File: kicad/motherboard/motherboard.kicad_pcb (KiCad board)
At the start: 2 copper layers, 88.9 x 80 mm, 33 parts, among them P1 CONN06, P10 CONN06, P11 CONN06, P12 CONN06, P13 CONN06, P14 CONN06, P15 CONN06, P16 CONN06, P17 CONN06, P18 CONN06, P19 CONN06, P2 CONN06, P20 CONN06, P21 CONN06, P22 CONN06, P23 CONN06, P24 CONN06, P25 CONN06, P26 CONN06, P27 CONN06, P28 CONN06, P29 CONN06, P3 CONN06, P30 CONN06, P31 CONN06, P32 CONN06, P4 CONN06, P5 CONN06, P6 CONN06, P7 CONN06, P8 CONN06, P9 CONN06

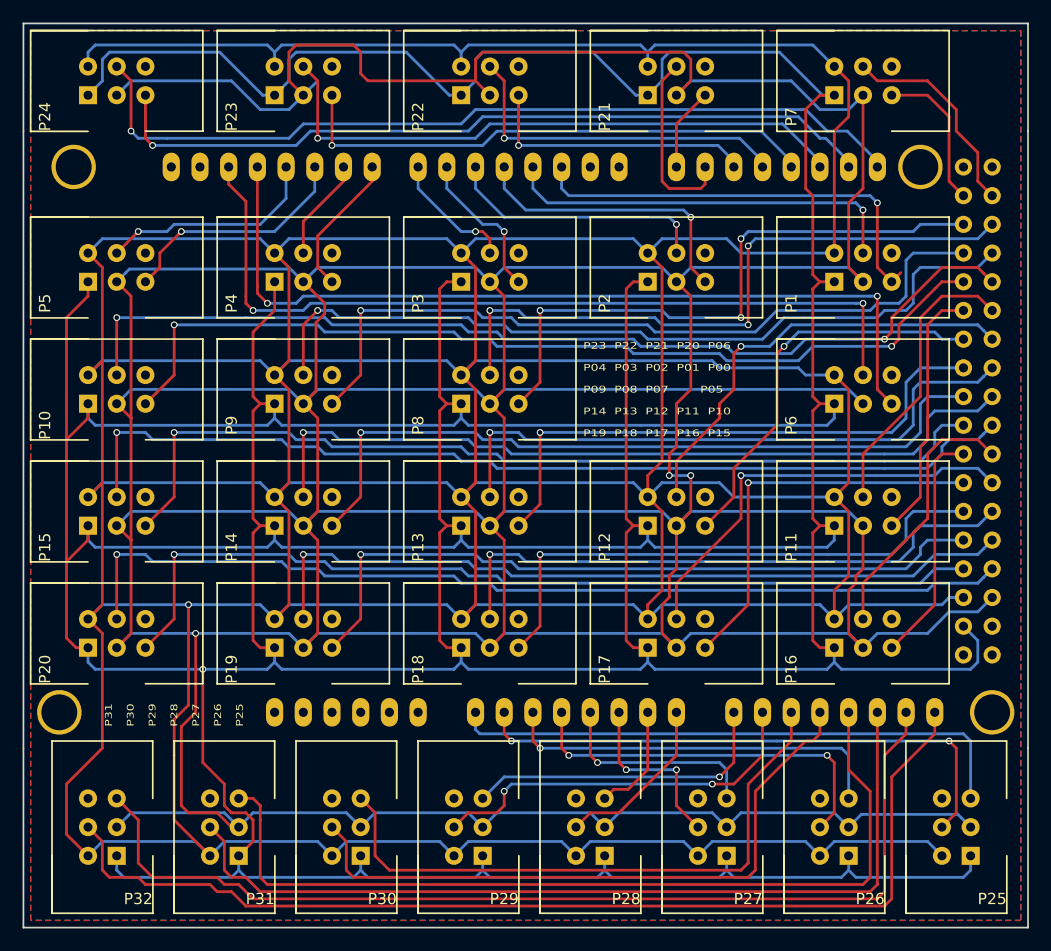
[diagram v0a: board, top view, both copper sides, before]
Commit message: Fix port references in Motherboard
So they match the port names
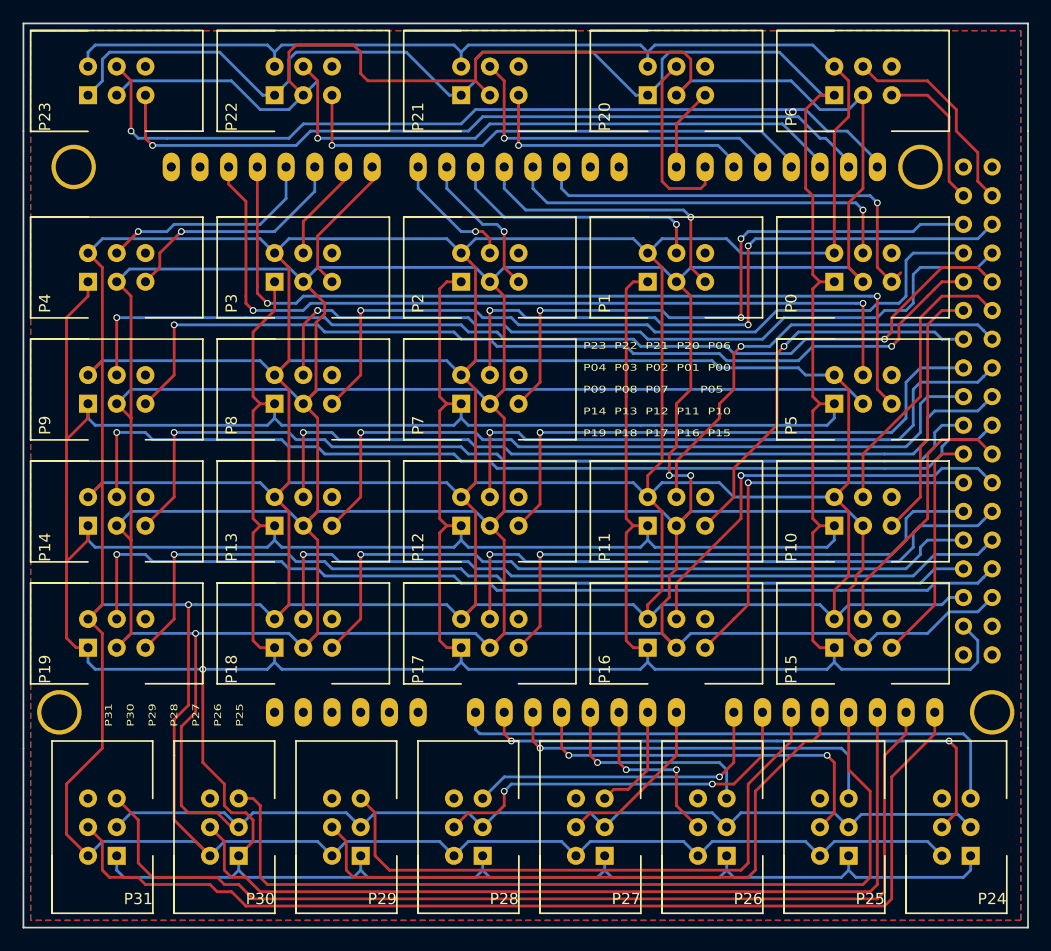
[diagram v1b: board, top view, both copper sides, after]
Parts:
- renumbered P1 to P0, P2 to P1, P11 to P10, P12 to P11, P13 to P12, P14 to P13, P15 to P14, P16 to P15, P17 to P16, P18 to P17, P19 to P18, P20 to P19, P3 to P2, P21 to P20, P22 to P21, P23 to P22, P24 to P23, P25 to P24, P26 to P25, P27 to P26, P28 to P27, P29 to P28, P30 to P29, P4 to P3, P31 to P30, P32 to P31, P5 to P4, P6 to P5, P7 to P6, P8 to P7, P9 to P8, P10 to P9

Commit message: Fix some aesthetical  paths in Motherboard
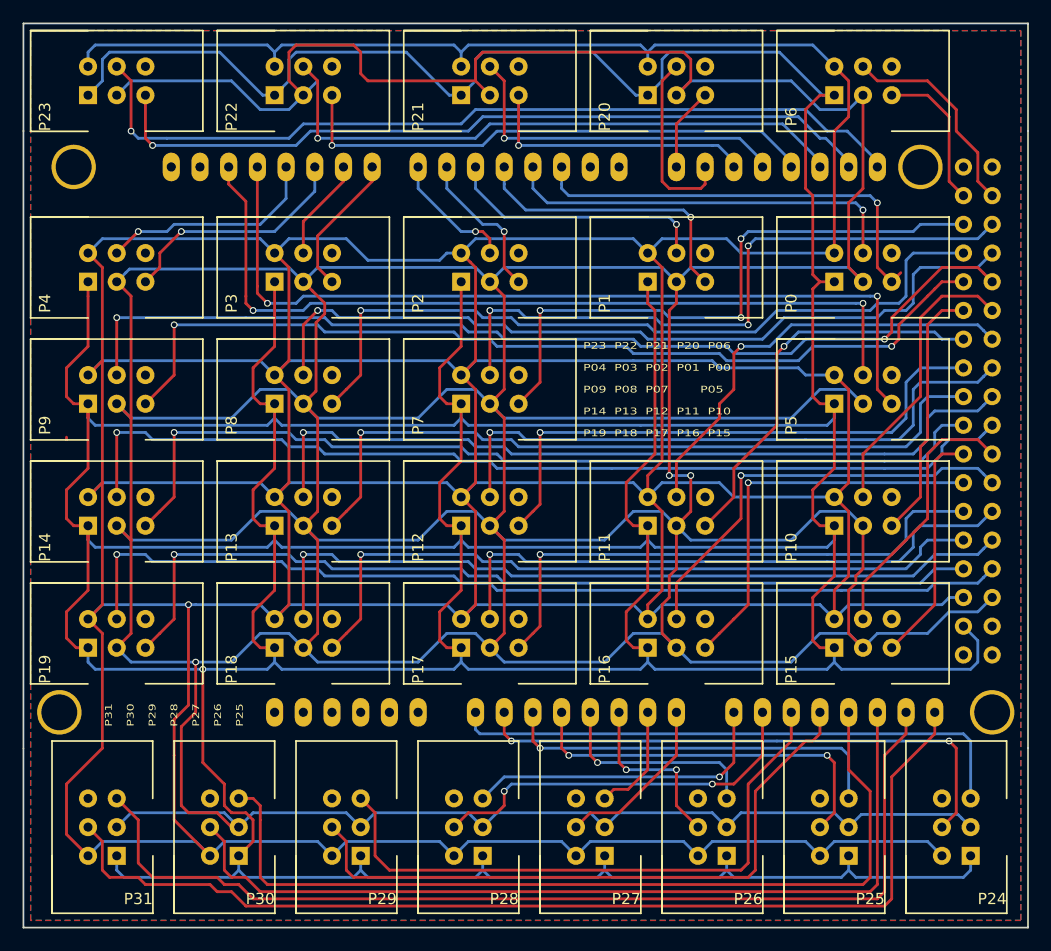
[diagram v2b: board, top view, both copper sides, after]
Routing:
- net MOSI: track 662.4 -> 670.4 mm
- net SCK: track 645.7 -> 647.7 mm
- net MISO: track 680.4 -> 680.9 mm

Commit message: Update plot settings for Motherboard
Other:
- board text added: "Avionica Motherboard for Arduino Mega - Rev.01"
- board text removed: "Avionica Motherboard Rev.01"
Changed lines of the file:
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@@
     (links 200)
     (no_connects 0)
-    (area 100.889999 74.854999 189.940001 155.015001)
+    (area 99.88 74.854999 189.940001 155.015001)
     (thickness 1.6)
     (drawings 12)
@@
     (visible_elements 7FFFF7FF)
     (pcbplotparams
-      (layerselection 0x010f0_80000001)
+      (layerselection 0x020f0_80000001)
       (usegerberextensions false)
       (excludeedgelayer true)
@@
   (gr_line (start 189.865 84.455) (end 189.865 139.065) (angle 90) (layer Edge.Cuts) (width 0.15))
   (gr_line (start 100.965 139.065) (end 100.965 84.455) (angle 90) (layer Edge.Cuts) (width 0.15))
-  (gr_text "Avionica Motherboard Rev.01\n" (at 187.96 152.4) (layer B.SilkS)
+  (gr_text "Avionica Motherboard for Arduino Mega - Rev.01\n" (at 187.96 152.4) (layer B.SilkS)
     (effects (font (size 1.016 1.016) (thickness 0.1905)) (justify left mirror))
   )
